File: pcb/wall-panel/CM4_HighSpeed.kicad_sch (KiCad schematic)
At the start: 41 parts, among them J5 F31L-1A7H1-11030, J6 690-019-298-412, U11 MT3608, U6 RT9742SNGV, U7 LP5907MFX-2.8

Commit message: wall panel v0.3
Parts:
- removed C32, C33: 22uF, Capacitor_SMD:C_0805_2012Metric, symbol Device:C_Small
- removed D3: B5817W, Diode_SMD:D_SOD-123, symbol Device:D
- removed JP5, JP6: SolderJumper_2_Bridged, Jumper:SolderJumper-2_P1.3mm_Bridged2Bar_Pad1.0x1.5mm, symbol Jumper:SolderJumper_2_Bridged
- removed JP7, JP8: 12.8/15V, Jumper:SolderJumper-3_P1.3mm_Bridged12_Pad1.0x1.5mm, symbol Jumper:SolderJumper_3_Bridged12
- removed L1: 10uH, Inductor_SMD:L_Taiyo-Yuden_NR-40xx, symbol Device:L_Small
- removed R17: 200K, Resistor_SMD:R_0402_1005Metric, symbol Device:R_Small
- removed R18, R29: 10K, Resistor_SMD:R_0402_1005Metric, symbol Device:R_Small
- removed R30: 240K, Resistor_SMD:R_0402_1005Metric, symbol Device:R_Small
- removed TP3: boost in, TestPoint:TestPoint_Pad_D1.5mm, symbol Connector:TestPoint
- removed TP4: boost out, TestPoint:TestPoint_Pad_D1.5mm, symbol Connector:TestPoint
- removed TP5: boost fb, TestPoint:TestPoint_Pad_D1.5mm, symbol Connector:TestPoint
- removed U11: MT3608, Package_TO_SOT_SMD:SOT-23-6, symbol Regulator_Switching:MT3608
- J5: value F31L-1A7H1-11030 -> SFV30R-4STBE1HLF; footprint F31L1A7H111030 -> SFV30R-4STBE1HLF:SFV30R4STBE1HLF; Height 2.75 -> 1.8; LCSC C3169750 -> C3168637; Manufacturer_Part_Number F31L-1A7H1-11030 -> SFV30R-4STBE1HLF; Mouser Part Number 649-F31L-1A7H1-11030 -> 649-SFV30R-4STBE1HLF; Mouser Price/Stock https://www.mouser.co.uk/ProductDetail/Amphenol-Aorora/F31L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 -> https://www.mouser.es/ProductDetail/Amphenol-FCI/SFV30R-4ST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
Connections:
- net BACKLIGHT_POWER_OUT renamed BACKLIGHT_POWER
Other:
- note removed: "input: 5v output: 12.8V or 15V output voltage is set by changing values of the r17 and r18 ideal values r17: 203k (rare find) r18: 10k"
- company: Grigorii Merkushev (aka brushknight) -> dotstar.tech
- title: Wall panel -> Wall Panel

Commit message: small fixes of v0.3.1
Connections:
- net DISPLAY_T: now reaches J5.7
- net DISPLAY_PWM: now reaches J5.8
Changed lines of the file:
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@@
 	(title_block
 		(title "Wall Panel")
-		(date "2026-02-02")
-		(rev "v0.3")
+		(date "2026-02-25")
+		(rev "v0.3.1")
 		(company "dotstar.tech")
 		(comment 1 "designed by Grigorii Merkushev (aka brushknight)")
@@
 		(effects
 			(font
+				(size 1.27 1.27)
+			)
+			(justify left)
+		)
+	)
+	(hierarchical_label "DISPLAY_PWM"
+		(shape input)
+		(at 180.34 45.72 0)
+		(effects
+			(font
+				(size 1.27 1.27)
+			)
+			(justify left)
+		)
+	)
+	(hierarchical_label "DISPLAY_T"
+		(shape input)
+		(at 180.34 43.18 0)
+		(effects
+			(font

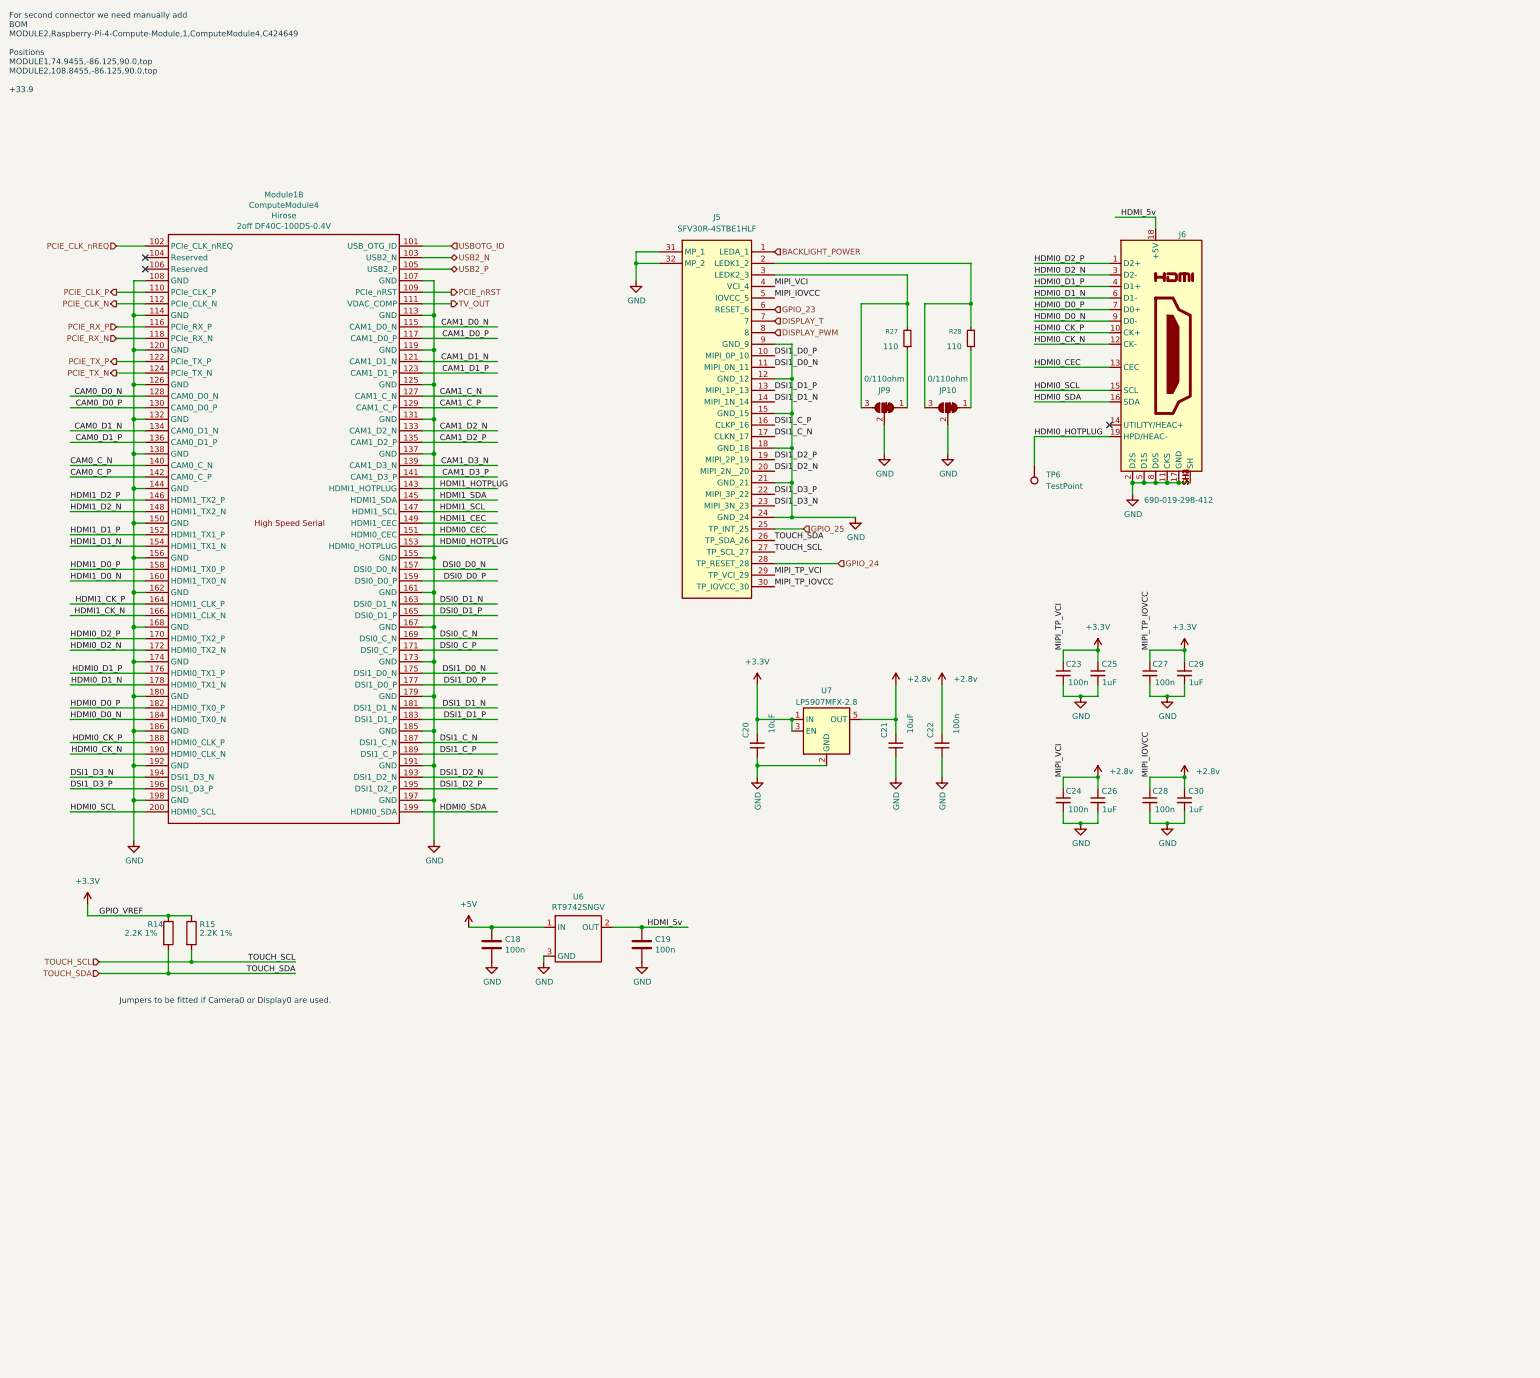
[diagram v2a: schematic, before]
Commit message: pogo pins wall panel
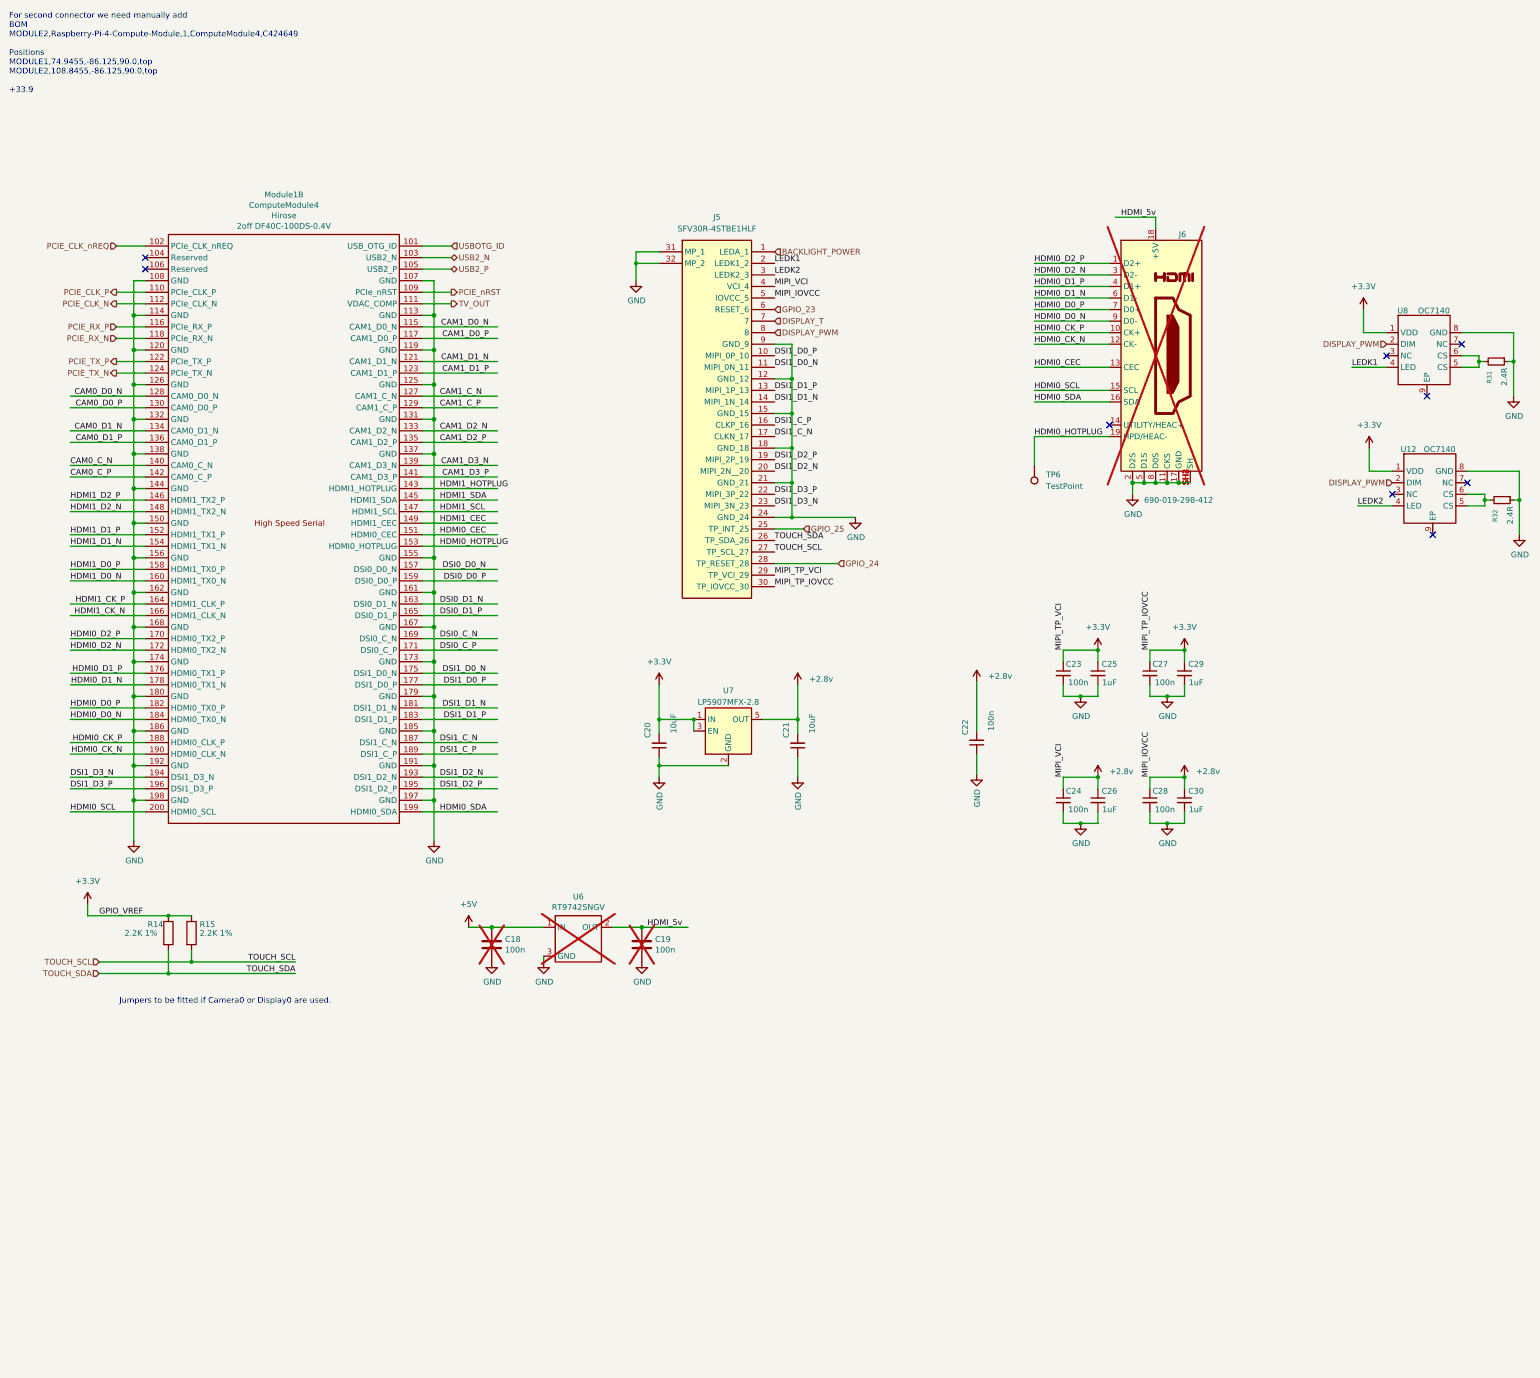
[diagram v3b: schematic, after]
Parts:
- removed JP10, JP9: 0/110ohm, Jumper:SolderJumper-3_P1.3mm_Bridged12_Pad1.0x1.5mm, symbol Jumper:SolderJumper_3_Bridged12
- removed R27, R28: 110, Resistor_SMD:R_0603_1608Metric, symbol Device:R_Small
- added R31, R32: 2.4R, Resistor_SMD:R_0603_1608Metric, symbol Device:R_Small
- added U12, U8: OC7140, OC7140:ESOP-8, symbol OC7140:OC7140
- C18, C19, J6, U6: now not fitted; now left out of the parts list
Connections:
- net +3.3V: now also U12.1 (VDD), U8.1 (VDD)
- net DISPLAY_PWM: now also U12.2 (DIM), U8.2 (DIM)
- net GND: now also R31.1, R32.1, U12.8 (GND), U8.8 (GND)
- net LEDK2: now reaches J5.3 (LEDK2_3)
- net LEDK2: now also U12.4 (LED)
- net LEDK1: now reaches J5.2 (LEDK1_2)
- net LEDK1: now also U8.4 (LED)
- new net: R31.2, U8.5 (CS), U8.6 (CS)
- new net: R32.2, U12.5 (CS), U12.6 (CS)
- no-connect marks 3 -> 9
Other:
- moved on the sheet: C20, C21, C22, U7
